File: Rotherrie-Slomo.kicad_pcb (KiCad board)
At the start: 2 copper layers, 99.6 x 19.4 mm, 43 parts, among them J1 CONN_02X05, J2 JACK_2P, J3 JACK_2P, J4 JACK_2P, J5 JACK_2P, U1 TL074, U2 TL074

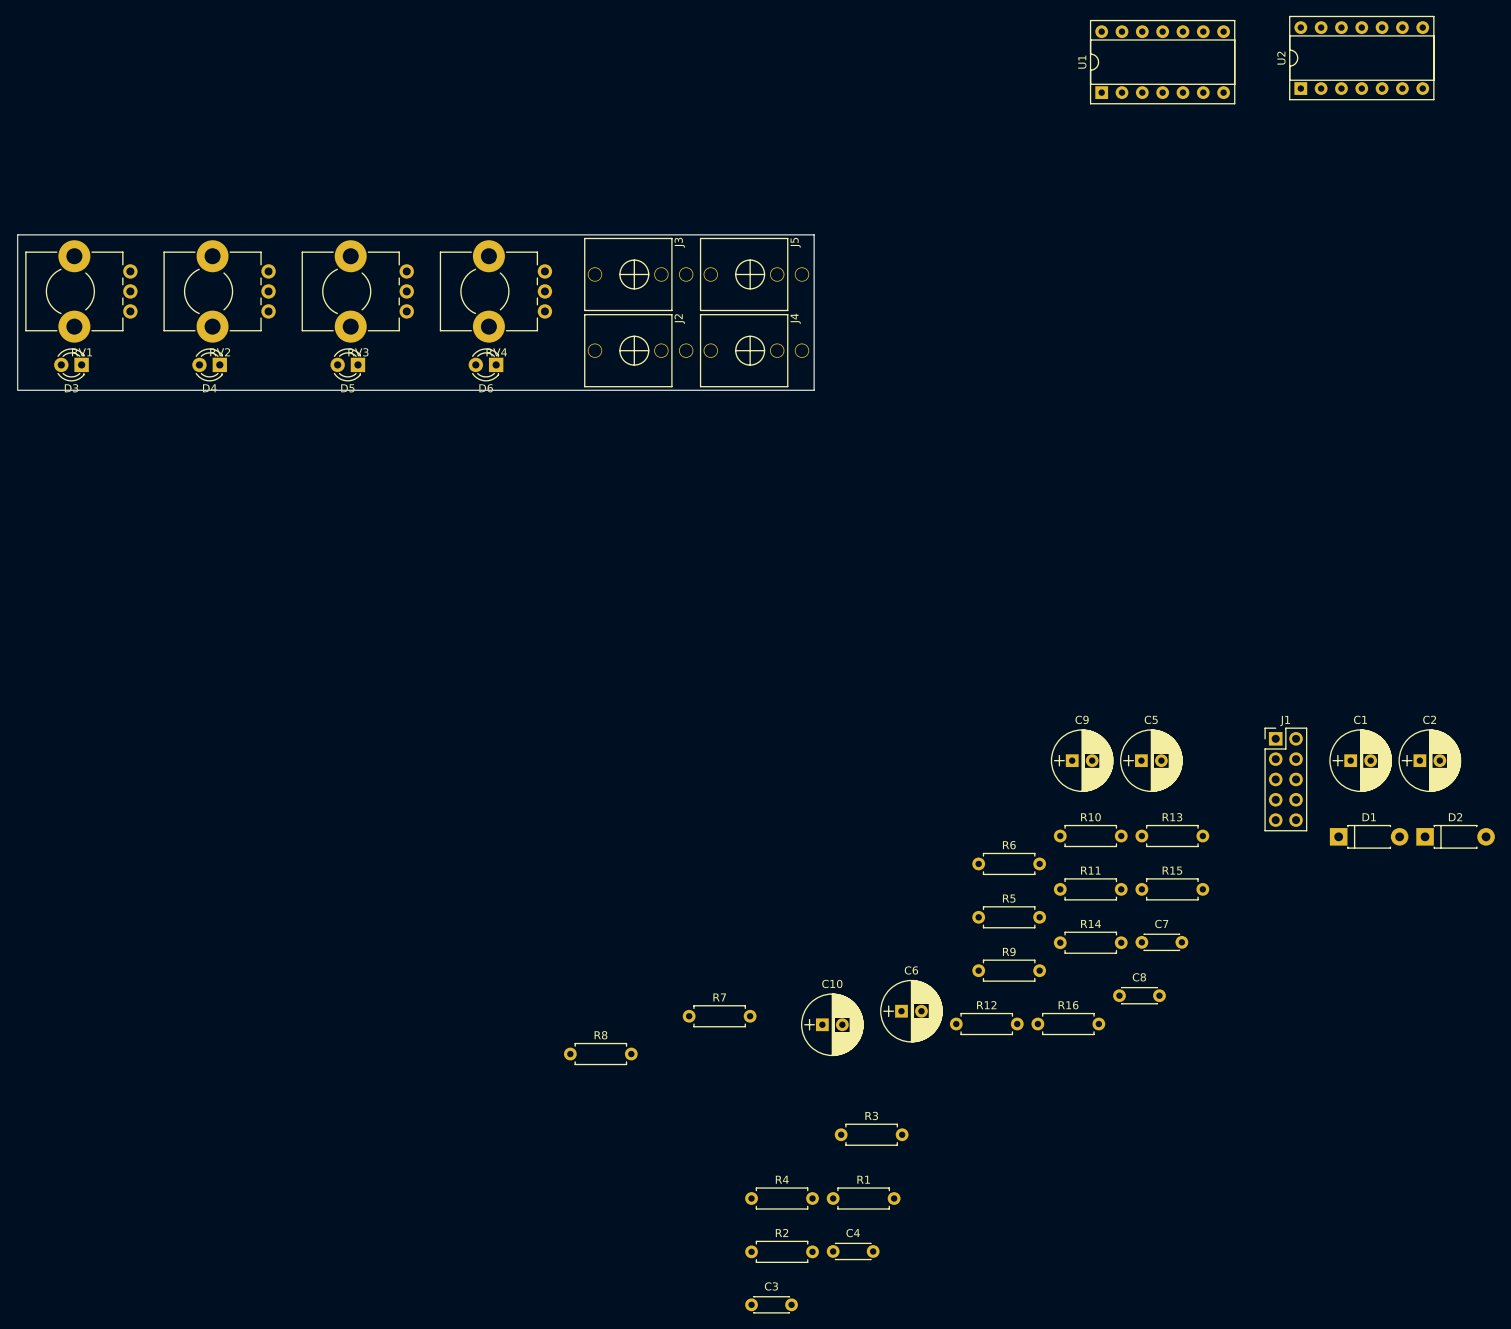
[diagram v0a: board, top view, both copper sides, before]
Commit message: Core board first setup
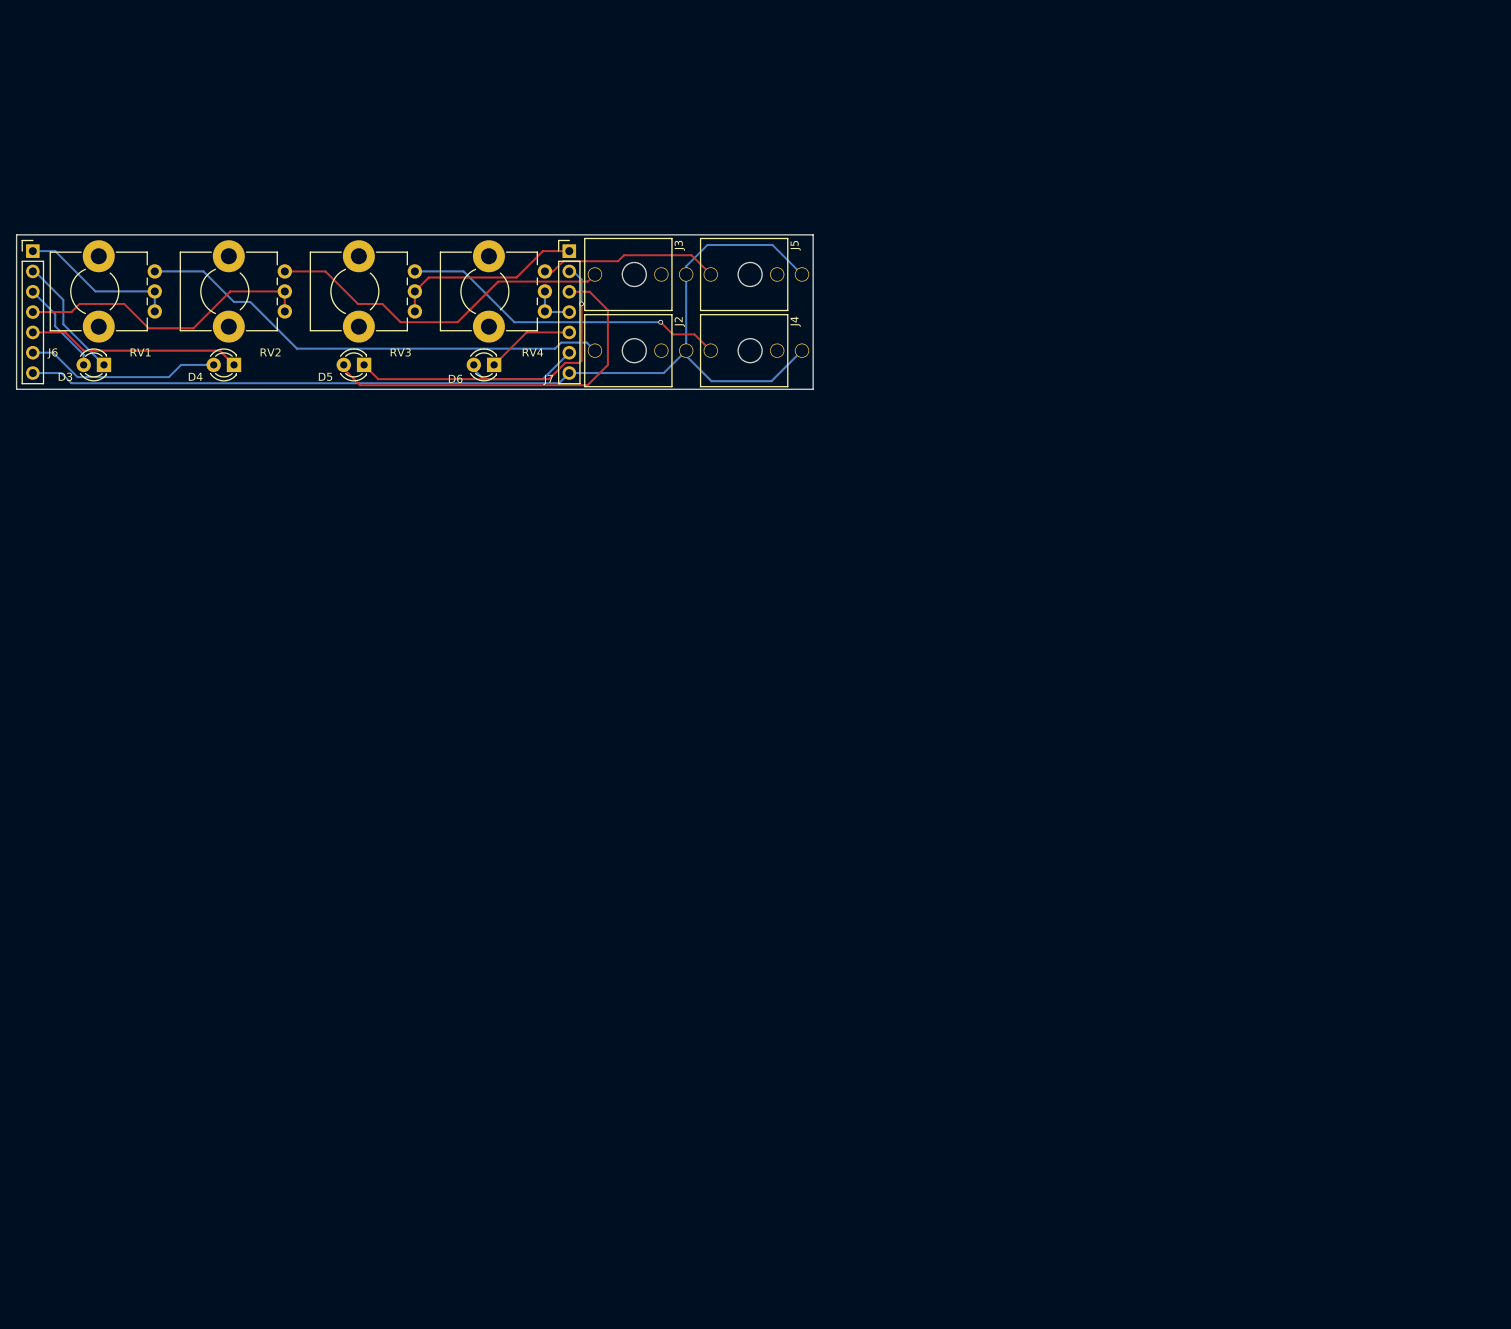
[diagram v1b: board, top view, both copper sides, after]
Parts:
- removed C1, C2: 22uF, Capacitors_THT:CP_Radial_D7.5mm_P2.50mm
- removed C10, C5, C6, C9: 100uF, Capacitors_THT:CP_Radial_D7.5mm_P2.50mm
- removed C3, C4, C7, C8: 100nF, Capacitors_THT:C_Disc_D4.3mm_W1.9mm_P5.00mm
- removed D1, D2: 1N5817, Diodes_THT:D_DO-41_SOD81_P7.62mm_Horizontal
- removed J1: CONN_02X05, Pin_Headers:Pin_Header_Straight_2x05_Pitch2.54mm
- removed R1, R2, R3, R4: 1k, Resistors_THT:R_Axial_DIN0207_L6.3mm_D2.5mm_P7.62mm_Horizontal
- removed R10, R11, R13, R14, R16, R5, R6, R9: 4.7k, Resistors_THT:R_Axial_DIN0207_L6.3mm_D2.5mm_P7.62mm_Horizontal
- removed R12, R15, R7, R8: 100k, Resistors_THT:R_Axial_DIN0207_L6.3mm_D2.5mm_P7.62mm_Horizontal
- removed U1, U2: TL074, Housings_DIP:DIP-14_W7.62mm_Socket
- added J6: CONN_01X07, Pin_Headers:Pin_Header_Straight_1x07_Pitch2.54mm, F.Cu at (83.3, 50.3)
- added J7: CONN_01X07, Pin_Headers:Pin_Header_Straight_1x07_Pitch2.54mm, F.Cu at (150.4, 50.3)
- J2, J3, J4, J5: footprint Eurocad:PJ301M-12 -> Eurocad:PJ301M-12-hole
- moved RV1 3.05 mm to (98.6, 52.8)
- moved D3 2.79 mm to (92.2, 64.5)
- moved RV2 2.03 mm to (114.8, 52.8)
- moved D4 1.78 mm to (108.5, 64.5)
- moved RV3 1.02 mm to (131.1, 52.8)
- moved D5 0.76 mm to (124.7, 64.5)
- moved D6 0.25 mm to (141.0, 64.5)
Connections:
- net Net-(R12-Pad2) renamed POT3
- net Net-(R15-Pad2) renamed POT4
- net Net-(R7-Pad2) renamed POT1
- net Net-(R8-Pad2) renamed POT2
- D3 pad 1: Net-(D3-Pad1) -> LED1
- D3 pad 2: Net-(D3-Pad2) -> LED1R
- D4 pad 1: Net-(D4-Pad1) -> LED2
- D4 pad 2: Net-(D4-Pad2) -> LED2R
- D5 pad 1: Net-(D5-Pad1) -> LED3
- D5 pad 2: Net-(D5-Pad2) -> LED3R
- D6 pad 1: Net-(D6-Pad1) -> LED4
- D6 pad 2: Net-(D6-Pad2) -> LED4R
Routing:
- net GND: track 0.00 -> 129.5 mm
- net WAVE1: track 0.00 -> 59.8 mm
- net LED3R: track 0.00 -> 48.1 mm
- net WAVE2: track 0.00 -> 43.9 mm
- net WAVE3: track 0.00 -> 41.1 mm, vias 0 -> 1
- net LED3: track 0.00 -> 41.0 mm, vias 0 -> 1
- net POT2: track 0.00 -> 37.6 mm
- net LED2: track 0.00 -> 26.8 mm
- net LED2R: track 0.00 -> 24.5 mm
- net POT3: track 0.00 -> 23.9 mm
- net WAVE4: track 0.00 -> 22.6 mm
- net POT1: track 0.00 -> 19.8 mm
- net LED1: track 0.00 -> 15.5 mm
- net LED4R: track 0.00 -> 14.4 mm
- net LED1R: track 0.00 -> 11.8 mm
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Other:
- board size 99.6 x 19.4 mm -> 99.6 x 19.3 mm

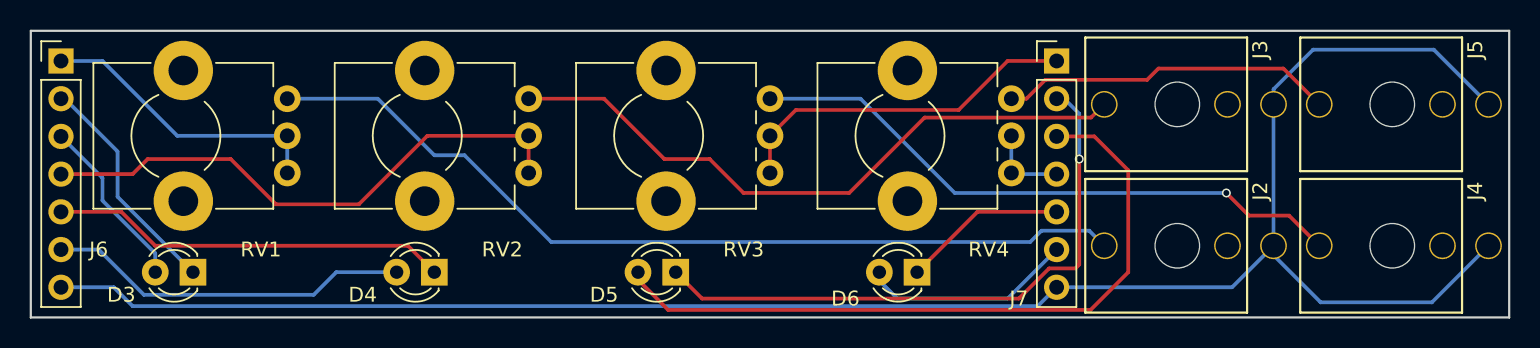
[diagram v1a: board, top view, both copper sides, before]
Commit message: Reroute controller board
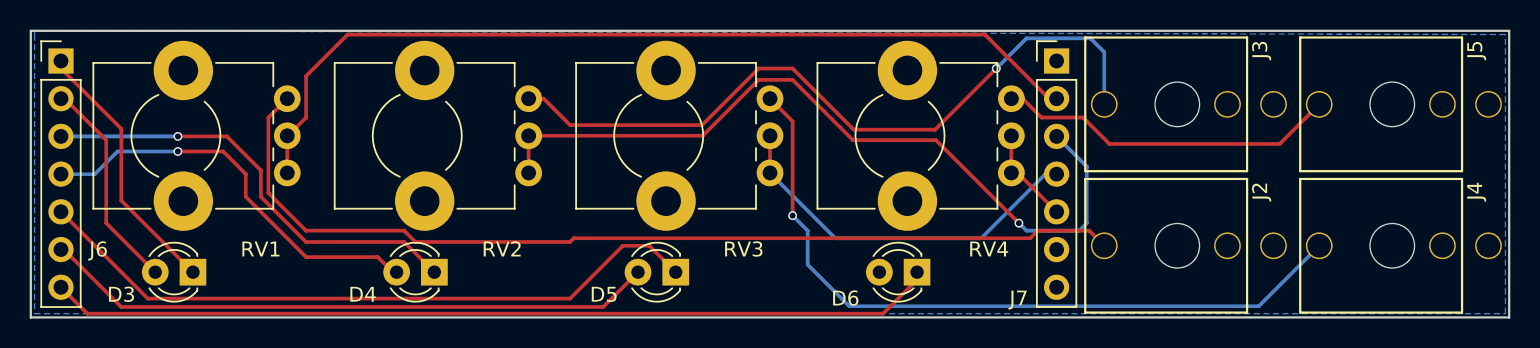
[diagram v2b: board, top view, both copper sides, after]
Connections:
- J6 pad 1: POT1 -> LED1
- J6 pad 2: LED1 -> LED1R
- J6 pad 3: LED1R -> LED2
- J6 pad 4: POT2 -> LED2R
- J6 pad 5: LED2 -> LED3
- J6 pad 6: LED2R -> LED3R
- J6 pad 7: GND -> LED4
- J7 pad 1: POT3 -> LED4R
- J7 pad 2: LED3 -> POT1
- J7 pad 3: LED3R -> POT2
- J7 pad 4: POT4 -> POT3
- J7 pad 5: LED4 -> POT4
- J7 pad 6: LED4R -> GND
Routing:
- net GND: track 129.5 -> 0.00 mm
- net LED4: track 11.1 -> 59.8 mm
- net POT1: track 19.8 -> 61.1 mm
- net POT2: track 37.6 -> 52.8 mm, vias 0 -> 1
- net LED4R: track 14.4 -> 0.57 mm
- net WAVE3: track 41.1 -> 49.5 mm
- net LED3R: track 48.1 -> 41.4 mm
- net WAVE1: track 59.8 -> 65.3 mm
- net WAVE2: track 43.9 -> 49.2 mm, vias 0 -> 1
- net LED3: track 41.0 -> 46.0 mm, vias 1 -> 0
- net LED2: track 26.8 -> 30.0 mm, vias 0 -> 1
- net LED2R: track 24.5 -> 27.5 mm, vias 0 -> 1
- net LED1R: track 11.8 -> 14.5 mm
- net LED1: track 15.5 -> 17.9 mm
- net POT3: track 23.9 -> 25.4 mm
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- added copper zone on B.Cu, net GND

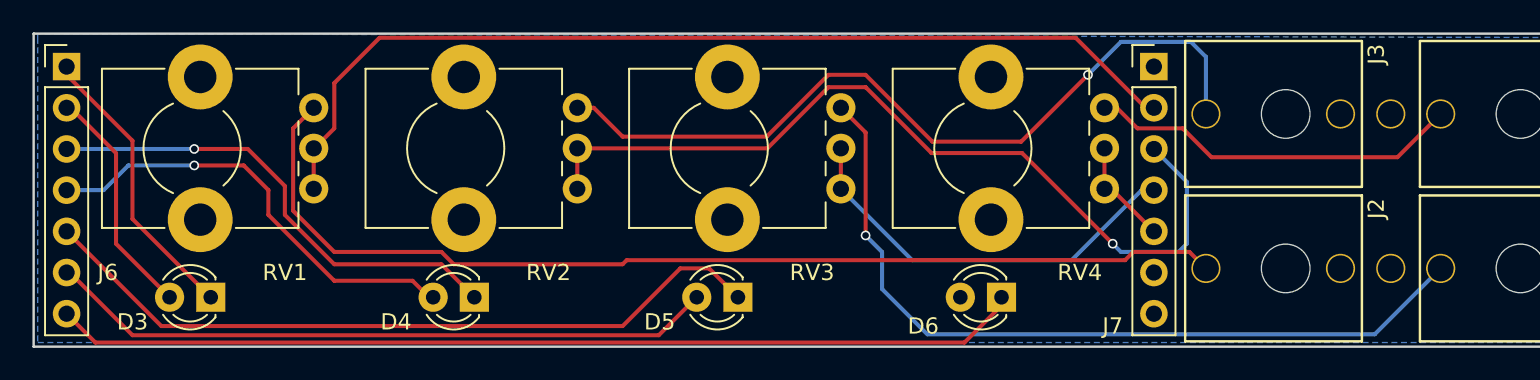
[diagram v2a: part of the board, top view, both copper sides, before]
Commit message: Controller board rerouted and added GND plane
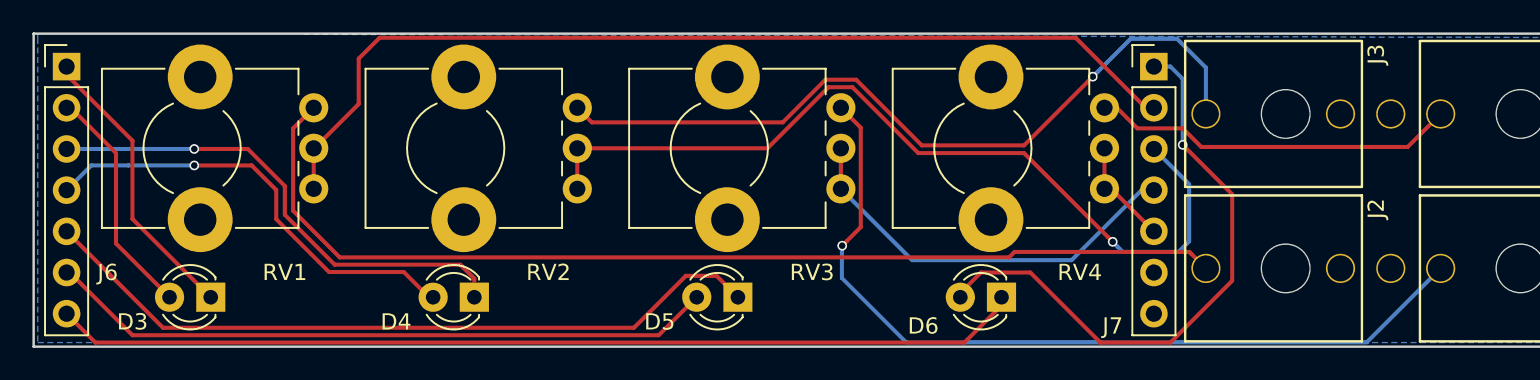
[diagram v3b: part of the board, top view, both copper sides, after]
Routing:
- net LED4R: track 0.57 -> 37.3 mm, vias 0 -> 1
- net WAVE3: track 49.5 -> 51.9 mm
- net WAVE2: track 49.2 -> 48.2 mm
- net LED2: track 30.0 -> 30.6 mm
- net WAVE4: track 23.1 -> 22.6 mm
